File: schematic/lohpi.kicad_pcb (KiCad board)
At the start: 4 copper layers, 65 x 56 mm, 198 parts, among them J1 CONN_01X02, J10 CONN_01X01, J11 CONN_01X01, J12 CONN_01X01, J13 CONN_01X01, J2 CONN_01X01, J3 CONN_01X01, J4 CONN_01X01, J5 CONN_01X01, J6 CONN_01X01, J7 UFL, J8 raspberry_pi_3_header, J9 CONN_01X02, Q1 Q_PMOS_GSD, U1 MCP1726-3302E/SN, U10 Anaren_B0430J50100AHF, U11 MurataSF2314E, U12 MurataSF2314E, U13 SPF5043Z, U14 RFPA0133TR7, U15 MurataSF2314E, U16 RFSW1012, U17 MurataSF2314E, U18 MAX-M8, U2 MCP1612, U3 MCP1726-3302E/SN, U4 MCP1824, U5 MCP1824, U6 MCP1824, U7 SX1301, U8 SX1257, U9 SX1257, X1 ABRACON-OSC, X2 ABRACON-OSC

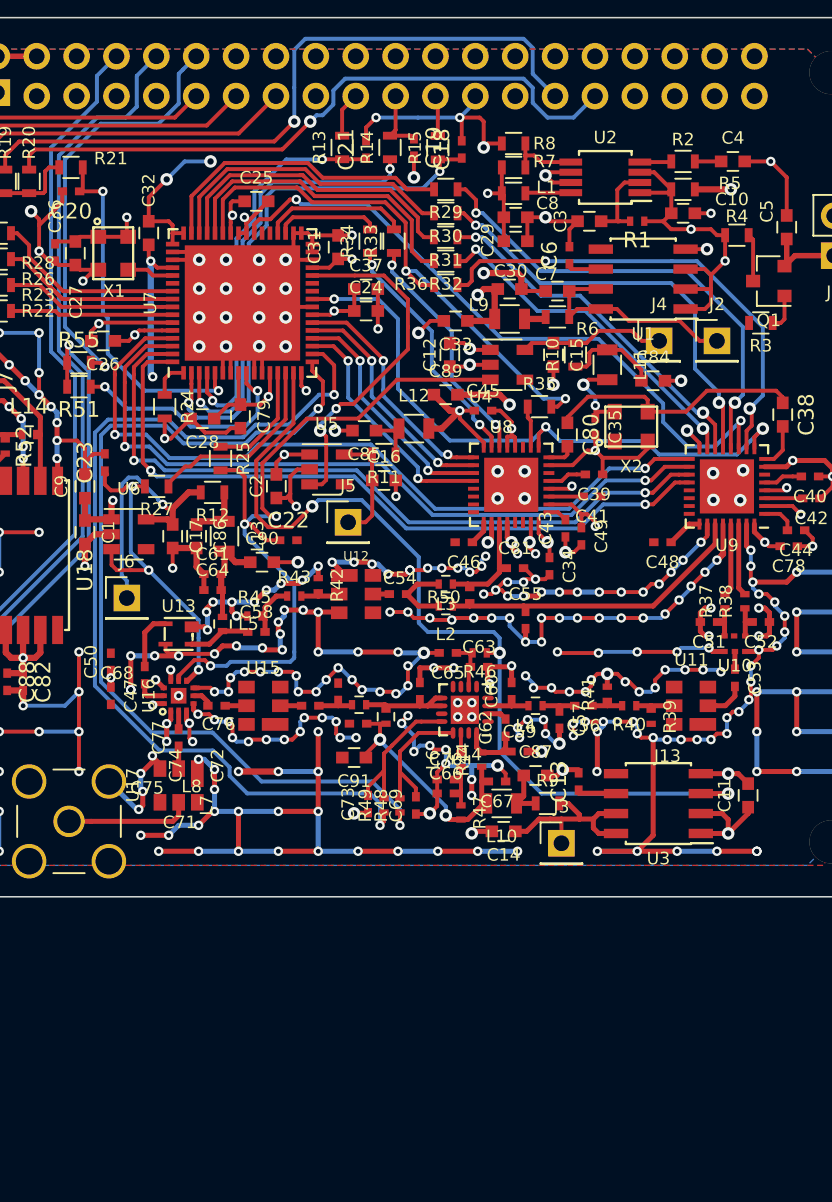
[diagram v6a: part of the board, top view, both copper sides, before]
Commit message: More updates to bom, added resistors to all communication lines
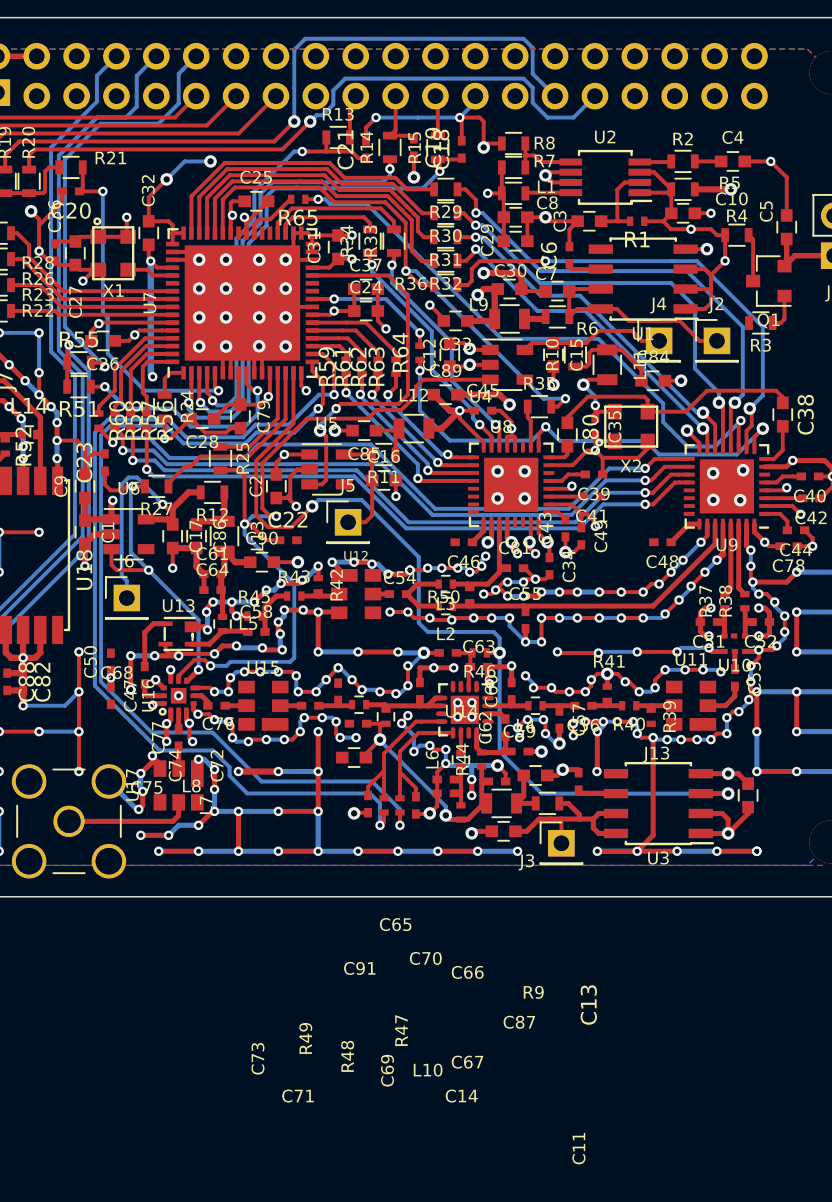
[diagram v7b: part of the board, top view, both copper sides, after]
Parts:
- added R56: 100, Resistors_SMD:R_0402_NoSilk, F.Cu at (105.9, 137.7)
- added R57: 100, Resistors_SMD:R_0402_NoSilk, F.Cu at (104.9, 137.7)
- added R58: 100, Resistors_SMD:R_0402_NoSilk, F.Cu at (103.9, 137.7)
- added R59: 100, Resistors_SMD:R_0402_NoSilk, F.Cu at (118.6, 134.2)
- added R60: 100, Resistors_SMD:R_0402_NoSilk, F.Cu at (102.9, 137.7)
- added R61: 100, Resistors_SMD:R_0402_NoSilk, F.Cu at (119.6, 134.2)
- added R62: 100, Resistors_SMD:R_0402_NoSilk, F.Cu at (120.7, 134.2)
- added R63: 100, Resistors_SMD:R_0402_NoSilk, F.Cu at (121.8, 134.2)
- added R64: 100, Resistors_SMD:R_0402_NoSilk, F.Cu at (123.3, 133.3)
- added R65: 100, Resistors_SMD:R_0402_NoSilk, F.Cu at (115.6, 123.6)
- moved R13 0.68 mm to (118.1, 119.6), turned to 0 degrees
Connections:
- J10 pad 1: Net-(J10-Pad1) -> (no net)
- J11 pad 1: Net-(J11-Pad1) -> (no net)
- J12 pad 1: Net-(J12-Pad1) -> (no net)
- J13 pad 1: Net-(J13-Pad1) -> (no net)
- J8 pad 1: (no net) -> Net-(J8-Pad1)
- J8 pad 16: (no net) -> Net-(J8-Pad16)
- J8 pad 17: (no net) -> Net-(J8-Pad17)
- J8 pad 18: (no net) -> Net-(J8-Pad18)
- J8 pad 22: (no net) -> Net-(J8-Pad22)
- J8 pad 24: (no net) -> Net-(J8-Pad24)
- J8 pad 26: (no net) -> Net-(J8-Pad26)
- J8 pad 27: (no net) -> Net-(J8-Pad27)
- J8 pad 28: (no net) -> Net-(J8-Pad28)
- J8 pad 3: (no net) -> Net-(J8-Pad3)
- J8 pad 32: (no net) -> Net-(J8-Pad32)
- J8 pad 33: (no net) -> Net-(J8-Pad33)
- J8 pad 35: (no net) -> Net-(J8-Pad35)
- J8 pad 36: (no net) -> Net-(J8-Pad36)
- J8 pad 37: (no net) -> Net-(J8-Pad37)
- J8 pad 38: (no net) -> Net-(J8-Pad38)
- J8 pad 40: (no net) -> Net-(J8-Pad40)
- J8 pad 5: (no net) -> Net-(J8-Pad5)
- J8 pad 7: (no net) -> Net-(J8-Pad7)
- U1 pad 5: (no net) -> Net-(U1-Pad5)
- U10 pad 5: Net-(U10-Pad5) -> (no net)
- U14 pad 1: Net-(U14-Pad1) -> (no net)
- U14 pad 11: Net-(U14-Pad11) -> (no net)
- U14 pad 15: Net-(U14-Pad15) -> (no net)
- U14 pad 4: Net-(U14-Pad4) -> (no net)
- U14 pad 5: Net-(U14-Pad5) -> (no net)
- U14 pad 7: Net-(U14-Pad7) -> (no net)
- U14 pad 8: Net-(U14-Pad8) -> (no net)
- U18 pad 13: (no net) -> Net-(U18-Pad13)
- U18 pad 15: (no net) -> Net-(U18-Pad15)
- U18 pad 16: (no net) -> Net-(U18-Pad16)
- U18 pad 17: (no net) -> Net-(U18-Pad17)
- U18 pad 18: (no net) -> Net-(U18-Pad18)
- U18 pad 5: (no net) -> Net-(U18-Pad5)
- U18 pad 9: (no net) -> Net-(U18-Pad9)
- U3 pad 5: (no net) -> Net-(U3-Pad5)
- U4 pad 4: (no net) -> Net-(U4-Pad4)
- U5 pad 4: (no net) -> Net-(U5-Pad4)
- U6 pad 4: (no net) -> Net-(U6-Pad4)
- U7 pad 19: /main_receiver/B_NSS -> Net-(R59-Pad2)
- U7 pad 20: /main_receiver/B_MOSI -> Net-(R61-Pad2)
- U7 pad 21: /main_receiver/B_MISO -> Net-(R62-Pad2)
- U7 pad 22: /main_receiver/B_SCK -> Net-(R63-Pad2)
- U7 pad 25: /main_receiver/RADIO_RST -> Net-(R64-Pad2)
- U7 pad 26: (no net) -> Net-(U7-Pad26)
- U7 pad 27: (no net) -> Net-(U7-Pad27)
- U7 pad 37: (no net) -> Net-(U7-Pad37)
- U7 pad 38: (no net) -> Net-(U7-Pad38)
- U7 pad 39: /main_receiver/SP_CLK_IN -> Net-(R65-Pad2)
- U7 pad 54: /main_receiver/GPIO[4] -> (no net)
- U7 pad 61: /main_receiver/A_SCKL -> Net-(R60-Pad1)
- U7 pad 62: /main_receiver/A_MISO -> Net-(R58-Pad1)
- U7 pad 63: /main_receiver/A_MOSI -> Net-(R57-Pad1)
- U7 pad 64: /main_receiver/A_NSS -> Net-(R56-Pad1)
- U8 pad 11: (no net) -> Net-(U8-Pad11)
- U8 pad 21: (no net) -> Net-(U8-Pad21)
- U8 pad 22: (no net) -> Net-(U8-Pad22)
- U8 pad 23: (no net) -> Net-(U8-Pad23)
- U8 pad 24: (no net) -> Net-(U8-Pad24)
- U8 pad 29: (no net) -> Net-(U8-Pad29)
- U8 pad 30: (no net) -> Net-(U8-Pad30)
- U8 pad 6: (no net) -> Net-(U8-Pad6)
- U9 pad 21: (no net) -> Net-(U9-Pad21)
- U9 pad 22: (no net) -> Net-(U9-Pad22)
- U9 pad 23: (no net) -> Net-(U9-Pad23)
- U9 pad 24: (no net) -> Net-(U9-Pad24)
- U9 pad 6: (no net) -> Net-(U9-Pad6)
- X2 pad 1: Net-(X2-Pad1) -> (no net)
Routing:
- net /main_receiver/RADIO_RST: track 39.8 -> 30.6 mm
- net Net-(R64-Pad2): track 0.00 -> 8.57 mm, vias 0 -> 2
- net Net-(R60-Pad1): track 0.00 -> 7.76 mm
- net /main_receiver/A_SCKL: track 49.3 -> 42.1 mm
- net /main_receiver/A_MISO: track 47.7 -> 40.7 mm
- net Net-(R58-Pad1): track 0.00 -> 6.81 mm
- net Net-(R63-Pad2): track 0.00 -> 6.57 mm
- net /main_receiver/A_MOSI: track 47.0 -> 40.5 mm
- net /main_receiver/B_SCK: track 15.2 -> 8.86 mm
- net /main_receiver/A_NSS: track 45.9 -> 40.0 mm
- net Net-(R57-Pad1): track 0.00 -> 5.85 mm
- net /main_receiver/B_MISO: track 15.2 -> 9.79 mm
- net Net-(R62-Pad2): track 0.00 -> 5.22 mm
- net Net-(R56-Pad1): track 0.00 -> 5.11 mm
- net /main_receiver/B_MOSI: track 15.5 -> 11.0 mm
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
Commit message: Add the rest of the passive components to bom
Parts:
- L1: footprint Inductors_SMD:L_0603 -> Inductors_SMD:L_0805
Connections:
- J10 pad 1: (no net) -> Net-(J10-Pad1)
- J11 pad 1: (no net) -> Net-(J11-Pad1)
- J12 pad 1: (no net) -> Net-(J12-Pad1)
- J13 pad 1: (no net) -> Net-(J13-Pad1)
- J8 pad 1: Net-(J8-Pad1) -> (no net)
- J8 pad 16: Net-(J8-Pad16) -> (no net)
- J8 pad 17: Net-(J8-Pad17) -> (no net)
- J8 pad 18: Net-(J8-Pad18) -> (no net)
- J8 pad 22: Net-(J8-Pad22) -> (no net)
- J8 pad 24: Net-(J8-Pad24) -> (no net)
- J8 pad 26: Net-(J8-Pad26) -> (no net)
- J8 pad 27: Net-(J8-Pad27) -> (no net)
- J8 pad 28: Net-(J8-Pad28) -> (no net)
- J8 pad 3: Net-(J8-Pad3) -> (no net)
- J8 pad 32: Net-(J8-Pad32) -> (no net)
- J8 pad 33: Net-(J8-Pad33) -> (no net)
- J8 pad 35: Net-(J8-Pad35) -> (no net)
- J8 pad 36: Net-(J8-Pad36) -> (no net)
- J8 pad 37: Net-(J8-Pad37) -> (no net)
- J8 pad 38: Net-(J8-Pad38) -> (no net)
- J8 pad 40: Net-(J8-Pad40) -> (no net)
- J8 pad 5: Net-(J8-Pad5) -> (no net)
- J8 pad 7: Net-(J8-Pad7) -> (no net)
- U1 pad 5: Net-(U1-Pad5) -> (no net)
- U10 pad 5: (no net) -> Net-(U10-Pad5)
- U14 pad 1: (no net) -> Net-(U14-Pad1)
- U14 pad 11: (no net) -> Net-(U14-Pad11)
- U14 pad 15: (no net) -> Net-(U14-Pad15)
- U14 pad 4: (no net) -> Net-(U14-Pad4)
- U14 pad 5: (no net) -> Net-(U14-Pad5)
- U14 pad 7: (no net) -> Net-(U14-Pad7)
- U14 pad 8: (no net) -> Net-(U14-Pad8)
- U18 pad 13: Net-(U18-Pad13) -> (no net)
- U18 pad 15: Net-(U18-Pad15) -> (no net)
- U18 pad 16: Net-(U18-Pad16) -> (no net)
- U18 pad 17: Net-(U18-Pad17) -> (no net)
- U18 pad 18: Net-(U18-Pad18) -> (no net)
- U18 pad 5: Net-(U18-Pad5) -> (no net)
- U18 pad 9: Net-(U18-Pad9) -> (no net)
- U3 pad 5: Net-(U3-Pad5) -> (no net)
- U4 pad 4: Net-(U4-Pad4) -> (no net)
- U5 pad 4: Net-(U5-Pad4) -> (no net)
- U6 pad 4: Net-(U6-Pad4) -> (no net)
- U7 pad 26: Net-(U7-Pad26) -> (no net)
- U7 pad 27: Net-(U7-Pad27) -> (no net)
- U7 pad 37: Net-(U7-Pad37) -> (no net)
- U7 pad 38: Net-(U7-Pad38) -> (no net)
- U7 pad 54: (no net) -> /main_receiver/GPIO[4]
- U8 pad 11: Net-(U8-Pad11) -> (no net)
- U8 pad 21: Net-(U8-Pad21) -> (no net)
- U8 pad 22: Net-(U8-Pad22) -> (no net)
- U8 pad 23: Net-(U8-Pad23) -> (no net)
- U8 pad 24: Net-(U8-Pad24) -> (no net)
- U8 pad 29: Net-(U8-Pad29) -> (no net)
- U8 pad 30: Net-(U8-Pad30) -> (no net)
- U8 pad 6: Net-(U8-Pad6) -> (no net)
- U9 pad 21: Net-(U9-Pad21) -> (no net)
- U9 pad 22: Net-(U9-Pad22) -> (no net)
- U9 pad 23: Net-(U9-Pad23) -> (no net)
- U9 pad 24: Net-(U9-Pad24) -> (no net)
- U9 pad 6: Net-(U9-Pad6) -> (no net)
- X2 pad 1: (no net) -> Net-(X2-Pad1)
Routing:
- net Net-(L1-Pad1): track 2.91 -> 5.62 mm
- net Net-(R7-Pad2): track 4.59 -> 6.11 mm
